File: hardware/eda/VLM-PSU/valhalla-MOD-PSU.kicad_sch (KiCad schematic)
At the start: 31 parts, among them J1 MAINS, J2 DC, J3 GPIO, J4 POWER, Q1 IRF9Z34N, U1 N7805-1P, U2 MCP111-450E/TO

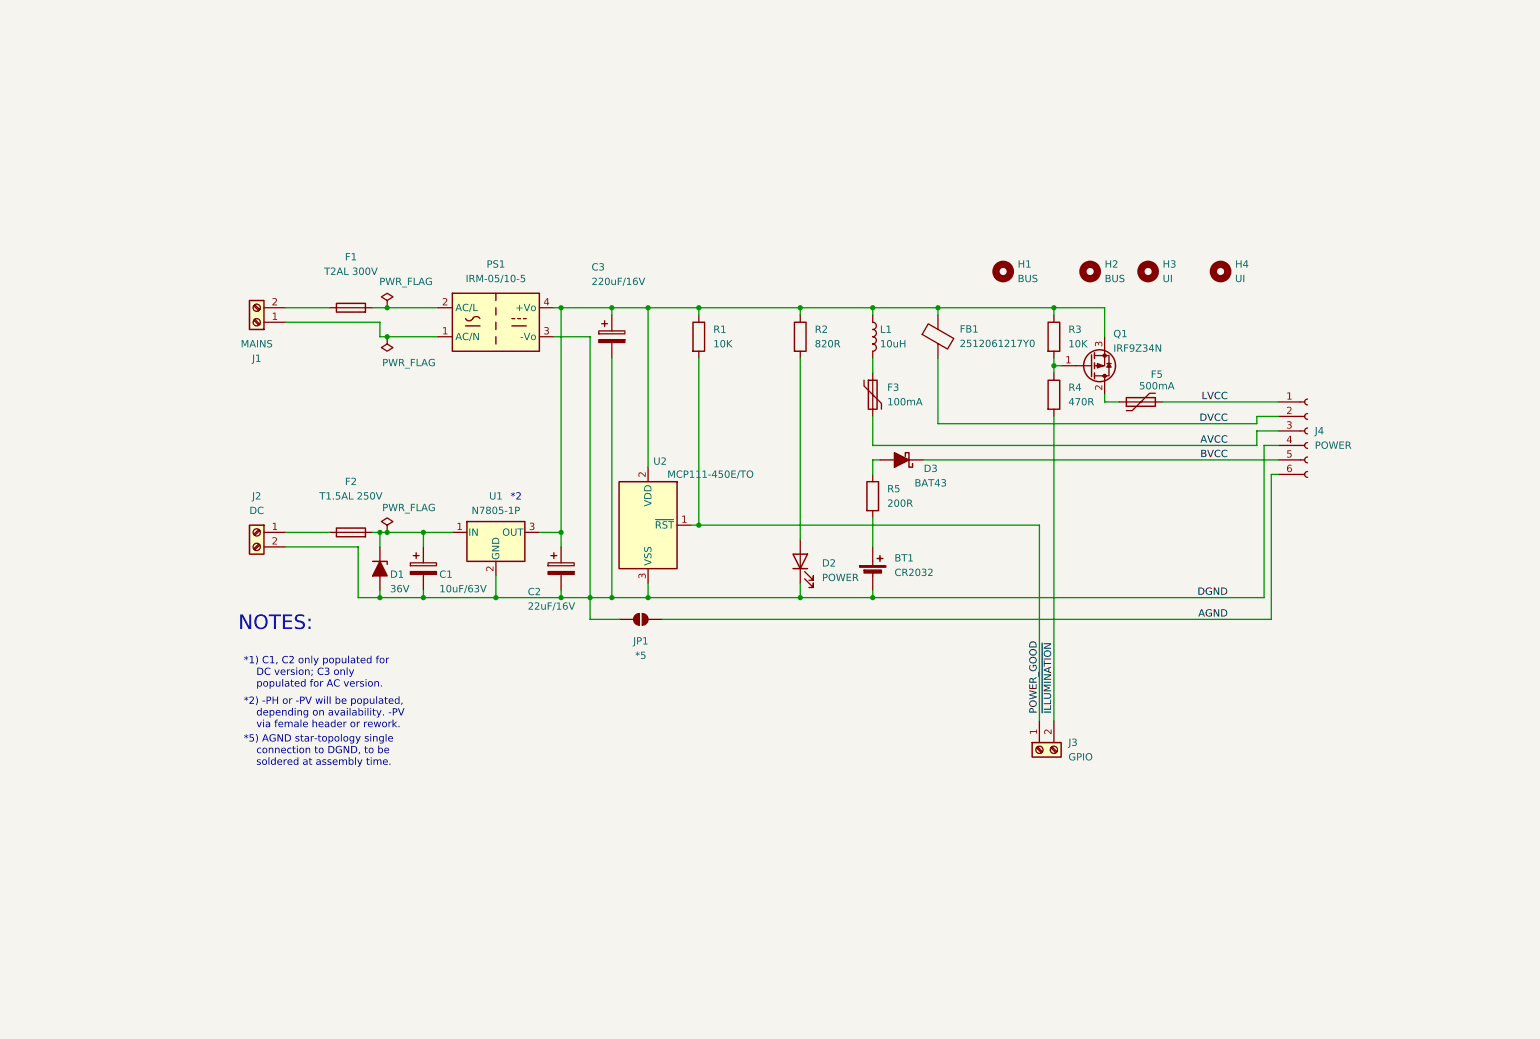
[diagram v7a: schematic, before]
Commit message: UPDATE: MOD-PSU revamped schematic should be done
 - allowed for all assembly variants:
  - single AC supply
  - single DC supply
  - dual AC/DC supply with ideal diode OR-ing
 - allowed for remote on/off option for both types of supplies
 - layout is next.
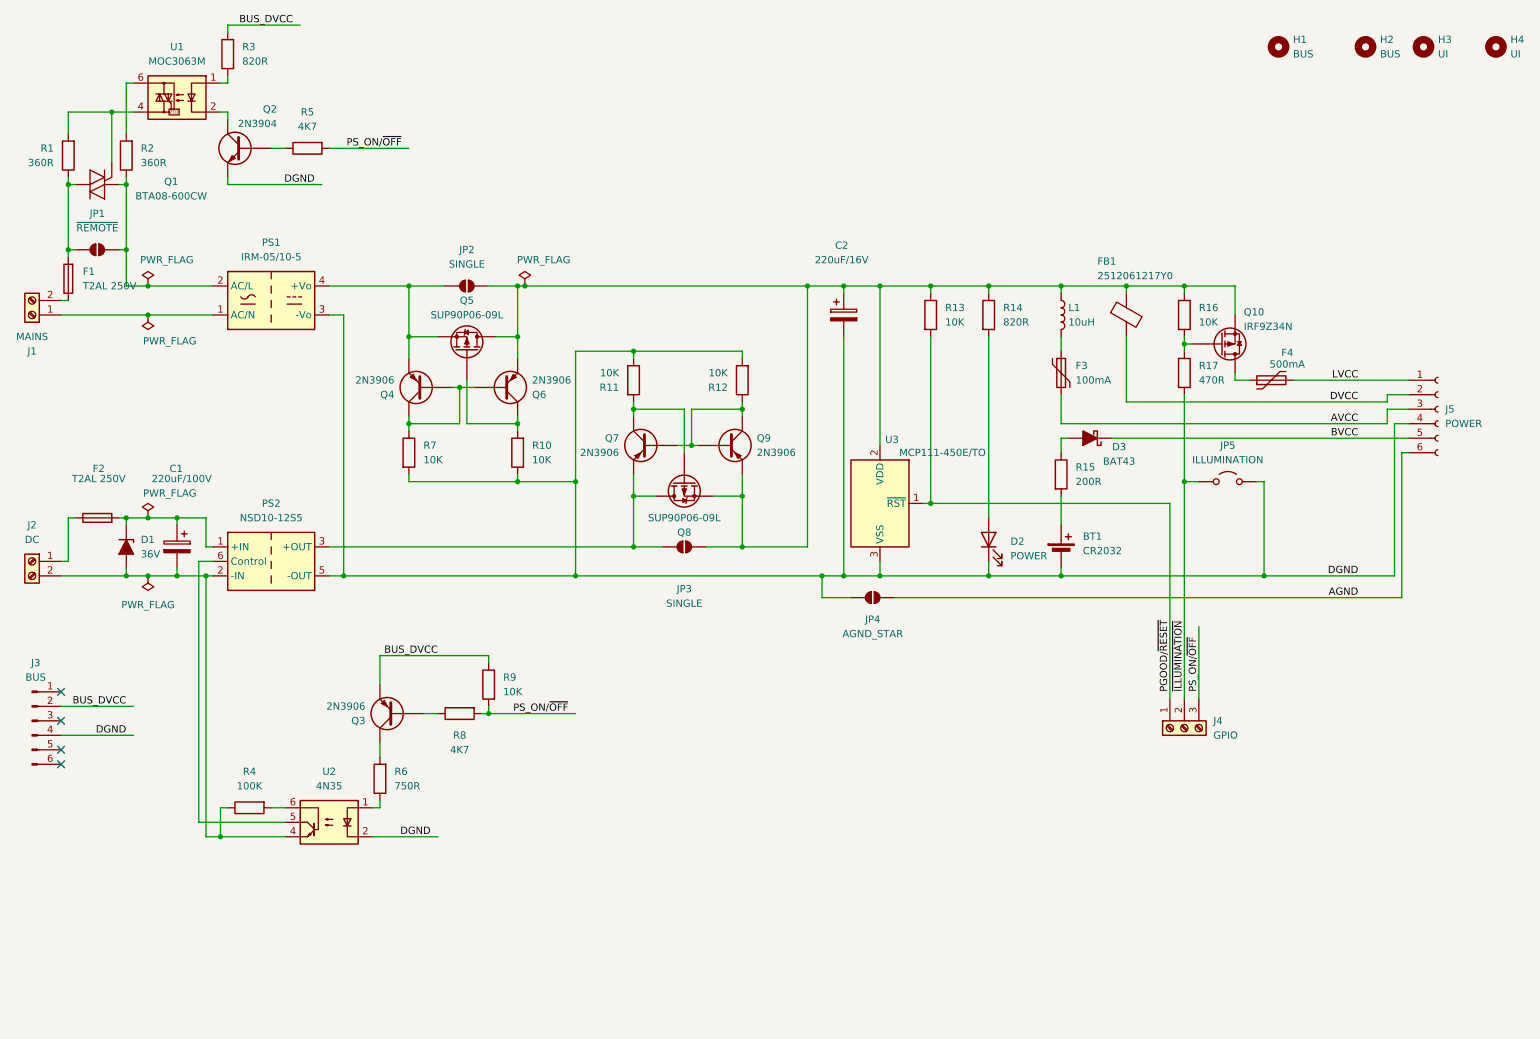
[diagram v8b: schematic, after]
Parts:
- removed C2: 22uF/16V, Capacitor_THT:CP_Radial_D5.0mm_P2.00mm, symbol Device:C_Polarized
- removed J3: GPIO, TerminalBlock_Phoenix:TerminalBlock_Phoenix_MPT-0,5-2-2.54_1x02_P2.54mm_Horizontal, symbol Connector:Screw_Terminal_01x02
- removed U1: N7805-1P, Package_TO_SOT_THT:TO-220-3_Horizontal_TabDown, symbol Regulator_Linear:L7805
- added J3: BUS, PCM_EasyEDA:Molex_KK-254_A-7478-06A_1x06_P2.54mm_Horizontal, symbol Connector:Conn_01x06_Pin
- added J4: GPIO, TerminalBlock_Phoenix:TerminalBlock_Phoenix_MPT-0,5-3-2.54_1x03_P2.54mm_Horizontal, symbol Connector:Screw_Terminal_01x03
- added JP1: ~{REMOTE}, Jumper:SolderJumper-2_P1.3mm_Open_TrianglePad1.0x1.5mm, symbol Jumper:SolderJumper_2_Open
- added JP2, JP3: SINGLE, Jumper:SolderJumper-2_P1.3mm_Open_TrianglePad1.0x1.5mm, symbol Jumper:SolderJumper_2_Open
- added JP5: ILLUMINATION, Connector_PinHeader_2.54mm:PinHeader_1x02_P2.54mm_Vertical, symbol Jumper:Jumper_2_Open
- added PS2: NSD10-12S5, Converter_DCDC:Converter_DCDC_MeanWell_NSD10_THT, symbol Converter_DCDC:NSD10-xxSyy
- added Q1: BTA08-600CW, Package_TO_SOT_THT:TO-220-3_Horizontal_TabDown, symbol Triac_Thyristor:BTA16-600CW
- added Q2: 2N3904, Package_TO_SOT_THT:TO-92_Wide, symbol Transistor_BJT:2N3904
- added Q3, Q4, Q6, Q7, Q9: 2N3906, Package_TO_SOT_THT:TO-92_Wide, symbol Transistor_BJT:2N3906
- added Q5, Q8: SUP90P06-09L, Package_TO_SOT_THT:TO-220-3_Horizontal_TabDown, symbol Transistor_FET:IRF4905
- added R1, R2: 360R, Resistor_THT:R_Axial_DIN0207_L6.3mm_D2.5mm_P5.08mm_Vertical, symbol Device:R
- added R10, R11, R12, R7, R9: 10K, Resistor_THT:R_Axial_DIN0207_L6.3mm_D2.5mm_P5.08mm_Vertical, symbol Device:R
- added R3: 820R, Resistor_THT:R_Axial_DIN0207_L6.3mm_D2.5mm_P5.08mm_Vertical, symbol Device:R
- added R4: 100K, Resistor_THT:R_Axial_DIN0207_L6.3mm_D2.5mm_P5.08mm_Vertical, symbol Device:R
- added R5, R8: 4K7, Resistor_THT:R_Axial_DIN0207_L6.3mm_D2.5mm_P5.08mm_Vertical, symbol Device:R
- added R6: 750R, Resistor_THT:R_Axial_DIN0207_L6.3mm_D2.5mm_P5.08mm_Vertical, symbol Device:R
- added U1: MOC3063M, Package_DIP:DIP-6_W10.16mm, symbol Relay_SolidState:MOC3063M
- added U2: 4N35, Package_DIP:DIP-6_W7.62mm, symbol Isolator:4N35
- BT1: footprint Battery:Battery_Panasonic_CR2032-HFN_Horizontal_CircularHoles -> PCM_EasyEDA:BAT-TH_BS-02-A1AJ010
- C1: value 10uF/63V -> 220uF/100V; footprint Capacitor_THT:CP_Radial_D5.0mm_P2.00mm -> Capacitor_THT:CP_Radial_D6.3mm_P2.50mm; Constraint (none) -> ESR < 1Ohm@350kHz
- F1: value T2AL 300V -> T2AL 250V
- F2: value T1.5AL 250V -> T2AL 250V
- JP4: renamed from JP1; value *5 -> AGND_STAR
- renumbered C3 to C2, F5 to F4, J4 to J5, Q1 to Q10, R1 to R13, R2 to R14, R5 to R15, R3 to R16, R4 to R17, U2 to U3
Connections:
- net DGND: now also J3.4 (Pin_4), JP5.2 (B), PS2.5 (-OUT), Q2.1 (E), R10.1, R11.1, R12.2, R7.2, U2.2; no longer C1.2, D1.2 (A), J2.2 (Pin_2)
- net ~{ILLUMINATION}: now also J4.2 (Pin_2), JP5.1 (A)
- net at C2.1, FB1.1, L1.1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: now also JP2.2 (B), JP3.2 (B), Q5.2 (D), Q6.1 (E), Q8.3 (S), Q9.1 (E); no longer PS1.4 (+Vo)
- net at F1.2: now also JP1.1 (A), Q1.2 (A2), R1.1; no longer PS1.2 (AC/L)
- net at C1.1, D1.1 (K), F2.2: now also PS2.1 (+IN)
- net POWER_GOOD renamed PGOOD/~{RESET}
- net PGOOD/~{RESET}: now also J4.1 (Pin_1)
- new net: C1.2, D1.2 (A), J2.2 (Pin_2), PS2.2 (-IN), R4.1, U2.4
- new net: JP3.1 (A), PS2.3 (+OUT), Q7.1 (E), Q8.2 (D)
- new net: PS2.6 (Control), U2.5
- new net: Q4.2 (B), Q4.3 (C), Q6.2 (B), R7.1
- new net: Q5.1 (G), Q6.3 (C), R10.2
- new net: R3.1, U1.1
- new net: JP2.1 (A), PS1.4 (+Vo), Q4.1 (E), Q5.3 (S)
- new net: Q7.2 (B), Q9.2 (B), Q9.3 (C), R12.1
- new net: Q7.3 (C), Q8.1 (G), R11.2
- new net: JP1.2 (B), PS1.2 (AC/L), Q1.1 (A1), R2.1
- new net: R2.2, U1.6
- new net: R6.1, U2.1
- new net: R4.2, U2.6
- new net: Q1.3 (G), R1.2, U1.4
- new net: Q2.2 (B), R5.1
- new net: Q3.3 (C), R6.2
- new net: Q3.2 (B), R8.1
- new net: Q2.3 (C), U1.2
- new net BUS_DVCC: J3.2 (Pin_2), Q3.1 (E), R3.2, R9.1
- new net PS_ON/~{OFF}: J4.3 (Pin_3), R5.2, R8.2, R9.2
- no-connect marks 0 -> 4
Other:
- note removed: "*1) C1, C2 only populated for DC version; C3 only populated for AC version."
- note removed: "*2"
- note removed: "*2) -PH or -PV will be populated, depending on availability. -PV via female header or rework."
- note removed: "*5) AGND star-topology single connection to DGND, to be soldered at assembly time."
- note removed: "NOTES:"
- moved on the sheet: BT1, C2, D2, D3, F1, F3, F4, FB1, H1, H2, H3, H4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
